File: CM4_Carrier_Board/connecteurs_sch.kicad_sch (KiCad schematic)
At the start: 2 parts, among them J2 DF40C-100DP-0.4V_51_, J3 DF40C-100DP-0.4V_51_

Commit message: Ajout de la sheet pour le PCIe
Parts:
- J2, J3: footprint HIROSE_DF40C-100DP-0.4V_51_ -> CM4_Carrier_Board:HIROSE_DF40C-100DP-0.4V_51_
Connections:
- net GND: now also J3.13, J3.14, J3.19, J3.20, J3.25, J3.26, J3.31, J3.32, J3.37, J3.38, J3.44, J3.50, J3.55, J3.56, J3.61, J3.62, J3.67, J3.68, J3.7, J3.73, J3.74, J3.79, J3.8, J3.80, J3.85, J3.86, J3.91, J3.92, J3.97, J3.98
- net PCIE/PCIe_CLK_P: now reaches J3.10
- net PCIE/PCIe_CLK_N: now reaches J3.12
- net PCIE/PCIe_RX_P: now reaches J3.16
- net PCIE/PCIe_RX_N: now reaches J3.18
- net PCIE/PCIe_CLK_nREQ: now reaches J3.2
- net PCIE/PCIe_TX_P: now reaches J3.22
- net PCIE/PCIe_TX_N: now reaches J3.24
- net USB_D_N: now reaches J3.3
- net HDMI_D2_P: now reaches J3.46
- net HDMI_D2_N: now reaches J3.48
- net USB_D_P: now reaches J3.5
- net HDMI_D1_P: now reaches J3.52
- net HDMI_D1_N: now reaches J3.54
- net HDMI_D0_P: now reaches J3.58
- net HDMI_D0_N: now reaches J3.60
- net HDMI_CLK_P: now reaches J3.64
- net HDMI_CLK_N: now reaches J3.66
- net PCIE/PCIe_nRST: now reaches J3.9
- no-connect marks 0 -> 122
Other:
- added sheet PCIE (PCIE.kicad_sch)

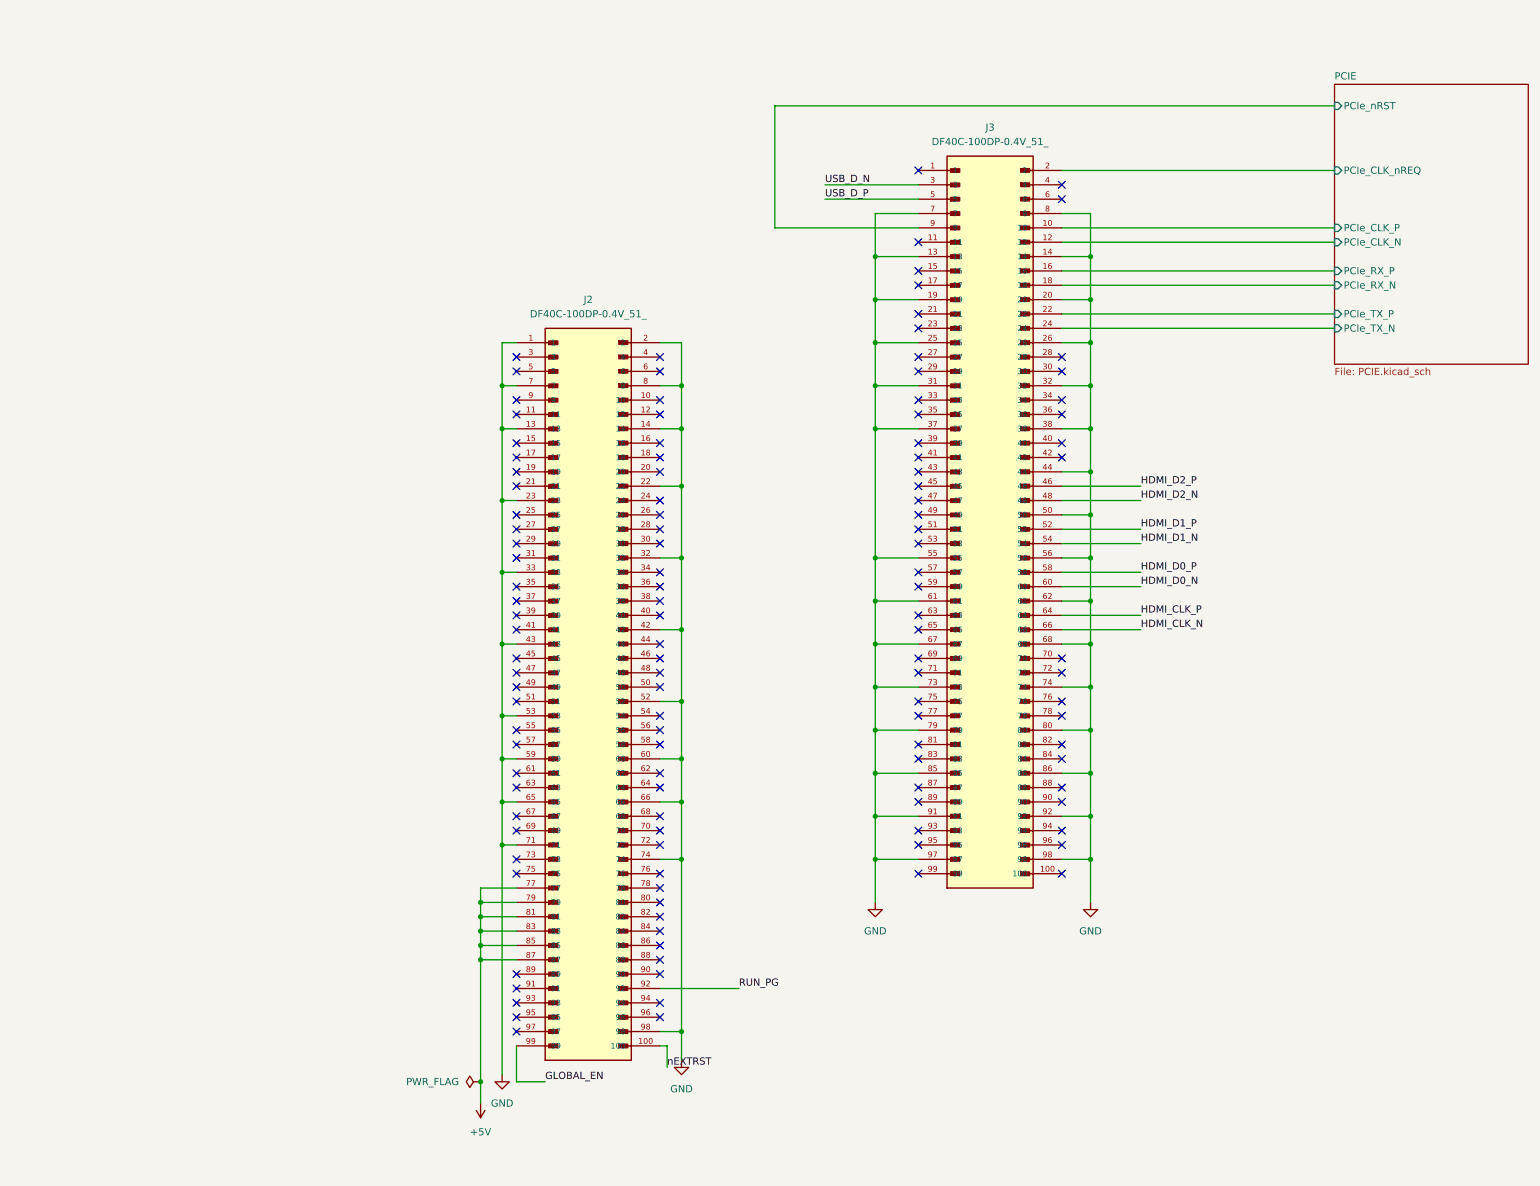
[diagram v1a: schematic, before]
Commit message: Implémentation du cavalier et de la diode d'activation des connecteurs, début d'implémentation du connecteur HDMI
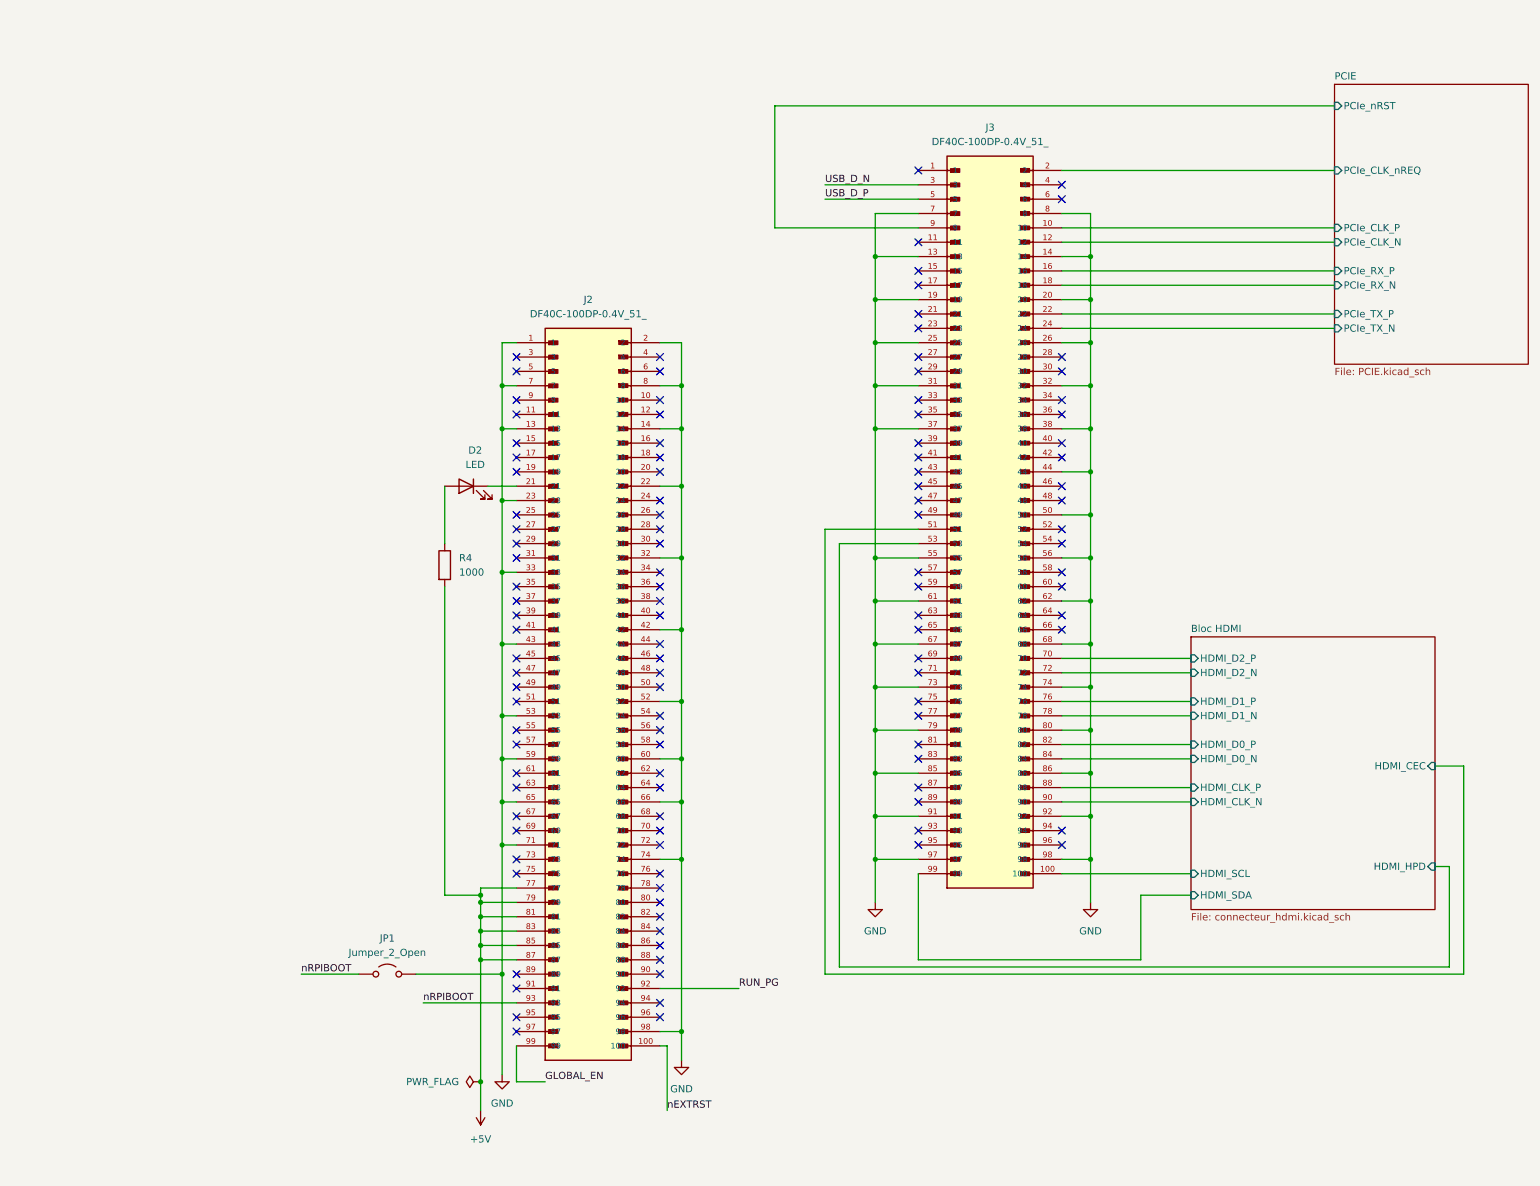
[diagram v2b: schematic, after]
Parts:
- added D2: LED, symbol Device:LED
- added JP1: Jumper_2_Open, symbol Jumper:Jumper_2_Open
- added R4: 1000, symbol Device:R
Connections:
- net +5V: now also R4.2
- net GND: now also JP1.2 (B)
- net Bloc HDMI/HDMI_SCL: now reaches J3.100
- net Bloc HDMI/HDMI_CEC: now reaches J3.51
- net Bloc HDMI/HDMI_HPD: now reaches J3.53
- net Bloc HDMI/HDMI_D2_P: now reaches J3.70
- net Bloc HDMI/HDMI_D2_N: now reaches J3.72
- net Bloc HDMI/HDMI_D1_P: now reaches J3.76
- net Bloc HDMI/HDMI_D1_N: now reaches J3.78
- net Bloc HDMI/HDMI_D0_P: now reaches J3.82
- net Bloc HDMI/HDMI_D0_N: now reaches J3.84
- net Bloc HDMI/HDMI_CLK_P: now reaches J3.88
- net Bloc HDMI/HDMI_CLK_N: now reaches J3.90
- net Bloc HDMI/HDMI_SDA: now reaches J3.99
- net at J2.21: now also D2.1 (K)
- net nRPIBOOT: now reaches J2.93
- net nRPIBOOT: now also JP1.1 (A)
- net HDMI_CLK_N: no longer names the net of J3.66
- net HDMI_CLK_P: no longer names the net of J3.64
- net HDMI_D0_N: no longer names the net of J3.60
- net HDMI_D0_P: no longer names the net of J3.58
- net HDMI_D1_N: no longer names the net of J3.54
- net HDMI_D1_P: no longer names the net of J3.52
- net HDMI_D2_N: no longer names the net of J3.48
- net HDMI_D2_P: no longer names the net of J3.46
- new net: D2.2 (A), R4.1
- no-connect marks 122 -> 116
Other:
- added sheet Bloc HDMI (connecteur_hdmi.kicad_sch)

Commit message: Implémentation bloc GPIO
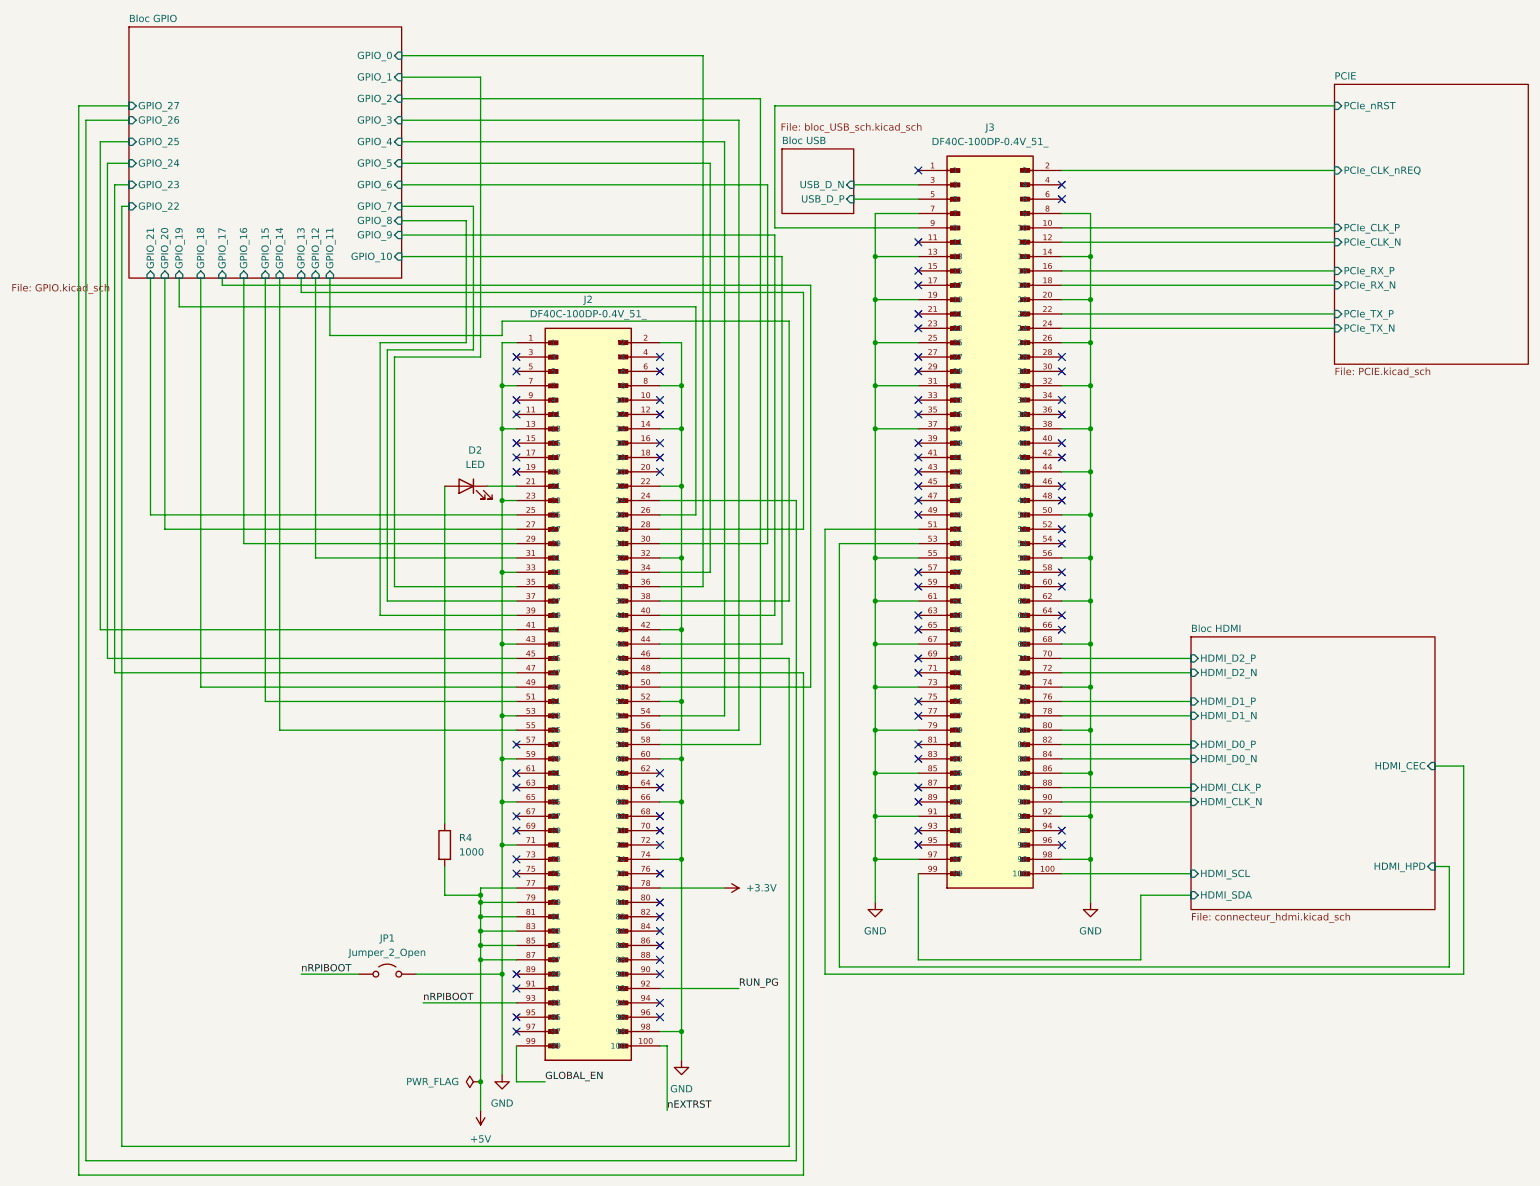
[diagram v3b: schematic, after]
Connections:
- net Bloc GPIO/GPIO_26: now reaches J2.24
- net Bloc GPIO/GPIO_21: now reaches J2.25
- net Bloc GPIO/GPIO_19: now reaches J2.26
- net Bloc GPIO/GPIO_20: now reaches J2.27
- net Bloc GPIO/GPIO_13: now reaches J2.28
- net Bloc GPIO/GPIO_16: now reaches J2.29
- net Bloc GPIO/GPIO_6: now reaches J2.30
- net Bloc GPIO/GPIO_12: now reaches J2.31
- net Bloc GPIO/GPIO_5: now reaches J2.34
- net Bloc GPIO/GPIO_1: now reaches J2.35
- net Bloc GPIO/GPIO_0: now reaches J2.36
- net Bloc GPIO/GPIO_7: now reaches J2.37
- net Bloc GPIO/GPIO_11: now reaches J2.38
- net Bloc GPIO/GPIO_8: now reaches J2.39
- net Bloc GPIO/GPIO_9: now reaches J2.40
- net Bloc GPIO/GPIO_25: now reaches J2.41
- net Bloc GPIO/GPIO_10: now reaches J2.44
- net Bloc GPIO/GPIO_24: now reaches J2.45
- net Bloc GPIO/GPIO_22: now reaches J2.46
- net Bloc GPIO/GPIO_23: now reaches J2.47
- net Bloc GPIO/GPIO_27: now reaches J2.48
- net Bloc GPIO/GPIO_18: now reaches J2.49
- net Bloc GPIO/GPIO_17: now reaches J2.50
- net Bloc GPIO/GPIO_15: now reaches J2.51
- net Bloc GPIO/GPIO_4: now reaches J2.54
- net Bloc GPIO/GPIO_14: now reaches J2.55
- net Bloc GPIO/GPIO_3: now reaches J2.56
- net Bloc GPIO/GPIO_2: now reaches J2.58
- net +3.3V: now reaches J2.78
- net USB_D_N renamed Bloc USB/USB_D_N
- net USB_D_P renamed Bloc USB/USB_D_P
- no-connect marks 116 -> 87
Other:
- added sheet Bloc GPIO (GPIO.kicad_sch)
- added sheet Bloc USB (bloc_USB_sch.kicad_sch)
- moved on the sheet: R4

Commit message: Assignement des empreintes et début du PCB
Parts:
- D2: footprint (none) -> LED_SMD:LED_0603_1608Metric
- JP1: footprint (none) -> Connector_PinHeader_2.54mm:PinHeader_1x02_P2.54mm_Vertical
- R4: footprint (none) -> Resistor_SMD:R_0603_1608Metric
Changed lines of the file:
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@@
 			)
 		)
-		(property "Footprint" ""
+		(property "Footprint" "Resistor_SMD:R_0603_1608Metric"
 			(at 64.262 149.86 90)
 			(hide yes)
@@
 			)
 		)
-		(property "Footprint" ""
+		(property "Footprint" "LED_SMD:LED_0603_1608Metric"
 			(at 69.85 86.36 0)
 			(hide yes)
@@
 			)
 		)
-		(property "Footprint" ""
+		(property "Footprint" "Connector_PinHeader_2.54mm:PinHeader_1x02_P2.54mm_Vertical"
 			(at 55.88 172.72 0)
 			(hide yes)
